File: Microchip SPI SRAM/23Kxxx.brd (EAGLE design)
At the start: 100 x 80 mm, 12 parts, among them IC2 23K**P, Q1 2SK1772

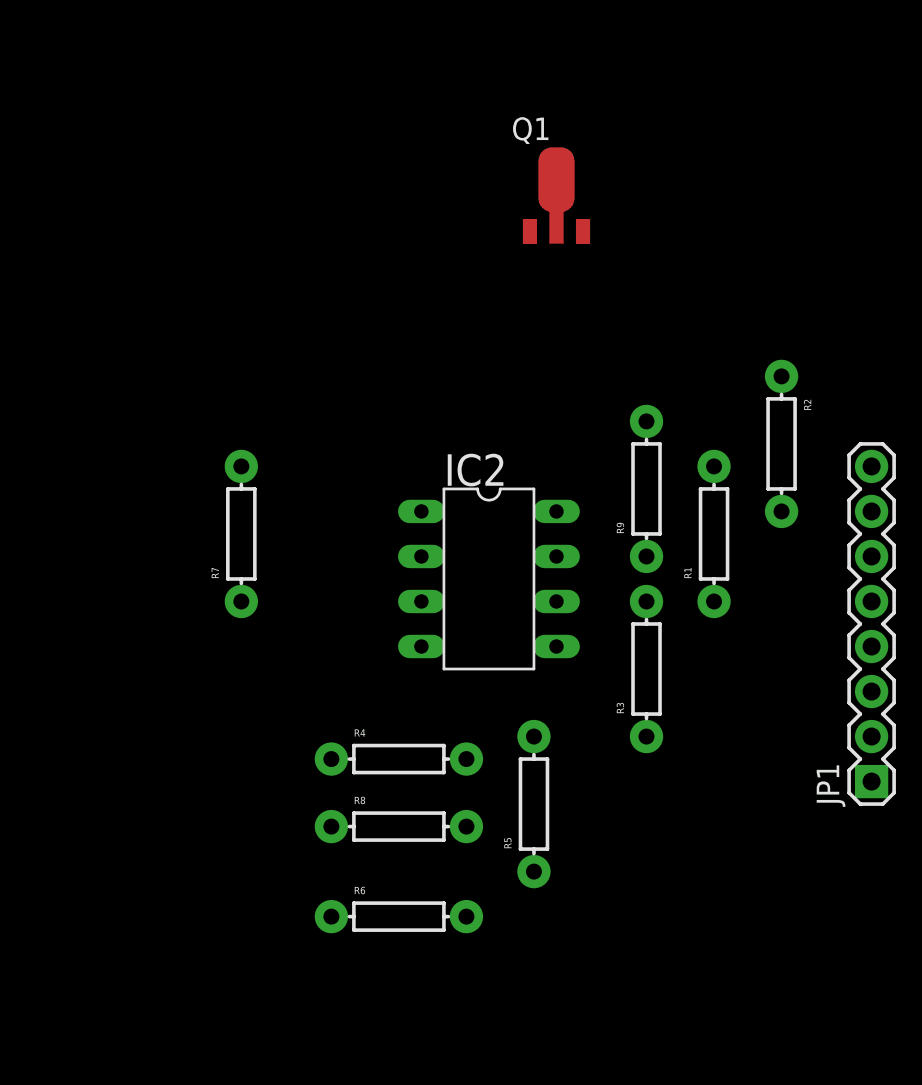
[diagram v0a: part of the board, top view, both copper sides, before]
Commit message: SPI SRAM pcb layout
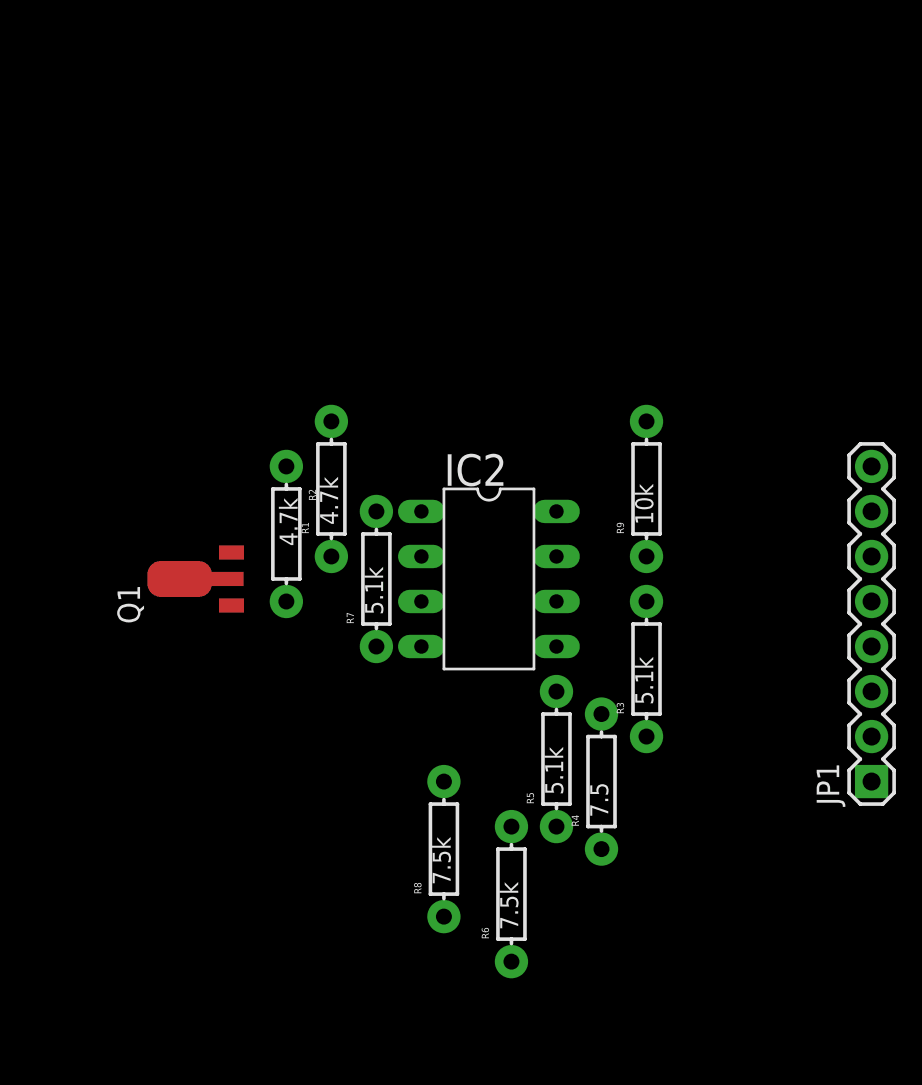
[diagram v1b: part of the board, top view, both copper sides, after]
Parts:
- R1, R2: value (none) -> 4.7k
- R3, R5, R7: value (none) -> 5.1k
- R4: value (none) -> 7.5
- R6, R8: value (none) -> 7.5k
- R9: value (none) -> 10k
- moved Q1 29.6 mm to (30.5, 30.5), turned to 90 degrees
- moved R2 28.4 mm to (35.6, 33.0)
- moved R1 21.7 mm to (38.1, 35.6)
- moved R4 11.5 mm to (53.3, 19.1), turned to 90 degrees
- moved R7 8.03 mm to (40.6, 30.5)
- moved R6 6.48 mm to (48.3, 12.7), turned to 90 degrees
- moved R8 2.84 mm to (44.5, 15.2), turned to 90 degrees
- moved R5 2.84 mm to (50.8, 20.3)
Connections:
- removed net N$2: JP1.3, Q1.3, R1.P$1
- new net N$1: JP1.3, Q1.2, Q1.2@1, R1.P$1
- net N$3: now also Q1.3; no longer Q1.2, Q1.2@1
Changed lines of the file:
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@@
 <elements>
 <element name="IC2" library="My Library" package="DIL8" value="23K**P" x="46.99" y="30.48" rot="R270"/>
-<element name="Q1" library="My Library" package="SOT89" value="2SK1772" x="50.8" y="52.07"/>
-<element name="R2" library="My Library" package="AXIAL-0.3" value="" x="63.5" y="38.1" rot="R270"/>
-<element name="R1" library="My Library" package="AXIAL-0.3" value="" x="59.69" y="33.02" rot="R90"/>
-<element name="R3" library="My Library" package="AXIAL-0.3" value="" x="55.88" y="25.4" rot="R90"/>
-<element name="R4" library="My Library" package="AXIAL-0.3" value="" x="41.91" y="20.32"/>
-<element name="R5" library="My Library" package="AXIAL-0.3" value="" x="49.53" y="17.78" rot="R90"/>
-<element name="R6" library="My Library" package="AXIAL-0.3" value="" x="41.91" y="11.43"/>
-<element name="R7" library="My Library" package="AXIAL-0.3" value="" x="33.02" y="33.02" rot="R90"/>
-<element name="R8" library="My Library" package="AXIAL-0.3" value="" x="41.91" y="16.51"/>
-<element name="R9" library="My Library" package="AXIAL-0.3" value="" x="55.88" y="35.56" rot="R90"/>
+<element name="Q1" library="My Library" package="SOT89" value="2SK1772" x="30.48" y="30.48" rot="R90"/>
+<element name="R2" library="My Library" package="AXIAL-0.3" value="4.7k" x="35.56" y="33.02" rot="R270"/>
+<element name="R1" library="My Library" package="AXIAL-0.3" value="4.7k" x="38.1" y="35.56" rot="R90"/>
+<element name="R3" library="My Library" package="AXIAL-0.3" value="5.1k" x="55.88" y="25.4" rot="R90"/>
+<element name="R4" library="My Library" package="AXIAL-0.3" value="7.5" x="53.34" y="19.05" rot="R90"/>
+<element name="R5" library="My Library" package="AXIAL-0.3" value="5.1k" x="50.8" y="20.32" rot="R90"/>
+<element name="R6" library="My Library" package="AXIAL-0.3" value="7.5k" x="48.26" y="12.7" rot="R90"/>
+<element name="R7" library="My Library" package="AXIAL-0.3" value="5.1k" x="40.64" y="30.48" rot="R90"/>
+<element name="R8" library="My Library" package="AXIAL-0.3" value="7.5k" x="44.45" y="15.24" rot="R90"/>
+<element name="R9" library="My Library" package="AXIAL-0.3" value="10k" x="55.88" y="35.56" rot="R90"/>
 <element name="JP1" library="SparkFun" package="1X08" value="" x="68.58" y="19.05" rot="R90"/>
 </elements>
@@
 <signal name="N$3">
 <contactref element="IC2" pad="2"/>
-<contactref element="Q1" pad="2"/>
-<contactref element="Q1" pad="2@1"/>
 <contactref element="R2" pad="P$1"/>
-<wire x1="50.8" y1="53.01" x2="50.8" y2="50.343" width="0" layer="19" extent="1-1"/>
-<wire x1="43.18" y1="31.75" x2="50.8" y2="50.343" width="0" layer="19" extent="1-1"/>
-<wire x1="63.5" y1="41.91" x2="50.8" y2="53.01" width="0" layer="19" extent="1-1"/>
+<contactref element="Q1" pad="3"/>
+<wire x1="35.56" y1="36.83" x2="43.18" y2="31.75" width="0" layer="19" extent="1-1"/>
+<wire x1="32.461" y1="31.979" x2="35.56" y2="36.83" width="0" layer="19" extent="1-1"/>
 </signal>
 <signal name="N$4">
 <contactref element="IC2" pad="1"/>
 <contactref element="R7" pad="P$2"/>
-<wire x1="33.02" y1="36.83" x2="43.18" y2="34.29" width="0" layer="19" extent="1-1"/>
+<wire x1="40.64" y1="34.29" x2="43.18" y2="34.29" width="0" layer="19" extent="1-1"/>
 </signal>
 <signal name="N$5">
@@
 <contactref element="JP1" pad="4"/>
 <wire x1="55.88" y1="21.59" x2="68.58" y2="26.67" width="0" layer="19" extent="1-1"/>
-<wire x1="45.72" y1="20.32" x2="55.88" y2="21.59" width="0" layer="19" extent="1-1"/>
+<wire x1="53.34" y1="22.86" x2="55.88" y2="21.59" width="0" layer="19" extent="1-1"/>
 </signal>
 <signal name="3.3V">
 <contactref element="Q1" pad="1"/>
-<contactref element="R2" pad="P$2"/>
 <contactref element="IC2" pad="8"/>
 <contactref element="R9" pad="P$2"/>
 <contactref element="JP1" pad="7"/>
-<wire x1="68.58" y1="34.29" x2="49.301" y2="50.089" width="0" layer="19" extent="1-1"/>
-<wire x1="63.5" y1="34.29" x2="68.58" y2="34.29" width="0" layer="19" extent="1-1"/>
-<wire x1="55.88" y1="39.37" x2="63.5" y2="34.29" width="0" layer="19" extent="1-1"/>
+<contactref element="R2" pad="P$2"/>
+<wire x1="55.88" y1="39.37" x2="68.58" y2="34.29" width="0" layer="19" extent="1-1"/>
 <wire x1="50.8" y1="34.29" x2="55.88" y2="39.37" width="0" layer="19" extent="1-1"/>
-</signal>
-<signal name="N$2">
-<contactref element="Q1" pad="3"/>
-<contactref element="R1" pad="P$1"/>
-<contactref element="JP1" pad="3"/>
-<wire x1="68.58" y1="24.13" x2="52.299" y2="50.089" width="0" layer="19" extent="1-1"/>
-<wire x1="59.69" y1="29.21" x2="68.58" y2="24.13" width="0" layer="19" extent="1-1"/>
+<wire x1="35.56" y1="29.21" x2="50.8" y2="34.29" width="0" layer="19" extent="1-1"/>
+<wire x1="32.461" y1="28.981" x2="35.56" y2="29.21" width="0" layer="19" extent="1-1"/>
 </signal>
 <signal name="5V">
 <contactref element="R1" pad="P$2"/>
 <contactref element="JP1" pad="8"/>
-<wire x1="68.58" y1="36.83" x2="59.69" y2="36.83" width="0" layer="19" extent="1-1"/>
+<wire x1="38.1" y1="39.37" x2="68.58" y2="36.83" width="0" layer="19" extent="1-1"/>
 </signal>
 <signal name="N$9">
 <contactref element="IC2" pad="5"/>
 <contactref element="R5" pad="P$2"/>
-<wire x1="49.53" y1="21.59" x2="50.8" y2="26.67" width="0" layer="19" extent="1-1"/>
+<wire x1="50.8" y1="24.13" x2="50.8" y2="26.67" width="0" layer="19" extent="1-1"/>
 </signal>
 <signal name="N$8">
@@
 <contactref element="R6" pad="P$2"/>
 <contactref element="JP1" pad="2"/>
-<wire x1="49.53" y1="13.97" x2="68.58" y2="21.59" width="0" layer="19" extent="1-1"/>
-<wire x1="45.72" y1="11.43" x2="49.53" y2="13.97" width="0" layer="19" extent="1-1"/>
+<wire x1="50.8" y1="16.51" x2="68.58" y2="21.59" width="0" layer="19" extent="1-1"/>
+<wire x1="48.26" y1="16.51" x2="50.8" y2="16.51" width="0" layer="19" extent="1-1"/>
 </signal>
 <signal name="N$11">
@@
 <contactref element="R8" pad="P$2"/>
 <contactref element="JP1" pad="1"/>
-<wire x1="45.72" y1="16.51" x2="68.58" y2="19.05" width="0" layer="19" extent="1-1"/>
-<wire x1="33.02" y1="29.21" x2="45.72" y2="16.51" width="0" layer="19" extent="1-1"/>
+<wire x1="44.45" y1="19.05" x2="68.58" y2="19.05" width="0" layer="19" extent="1-1"/>
+<wire x1="40.64" y1="26.67" x2="44.45" y2="19.05" width="0" layer="19" extent="1-1"/>
 </signal>
 <signal name="GND">
@@
 <contactref element="IC2" pad="4"/>
 <contactref element="JP1" pad="5"/>
-<wire x1="43.18" y1="26.67" x2="68.58" y2="29.21" width="0" layer="19" extent="1-1"/>
-<wire x1="38.1" y1="20.32" x2="43.18" y2="26.67" width="0" layer="19" extent="1-1"/>
-<wire x1="38.1" y1="16.51" x2="38.1" y2="20.32" width="0" layer="19" extent="1-1"/>
-<wire x1="38.1" y1="11.43" x2="38.1" y2="16.51" width="0" layer="19" extent="1-1"/>
+<wire x1="53.34" y1="15.24" x2="68.58" y2="29.21" width="0" layer="19" extent="1-1"/>
+<wire x1="48.26" y1="8.89" x2="53.34" y2="15.24" width="0" layer="19" extent="1-1"/>
+<wire x1="44.45" y1="11.43" x2="48.26" y2="8.89" width="0" layer="19" extent="1-1"/>
+<wire x1="43.18" y1="26.67" x2="53.34" y2="15.24" width="0" layer="19" extent="1-1"/>
+</signal>
+<signal name="N$1">
+<contactref element="JP1" pad="3"/>
+<contactref element="Q1" pad="2"/>
+<contactref element="Q1" pad="2@1"/>
+<contactref element="R1" pad="P$1"/>
+<wire x1="38.1" y1="31.75" x2="68.58" y2="24.13" width="0" layer="19" extent="1-1"/>
+<wire x1="32.207" y1="30.48" x2="38.1" y2="31.75" width="0" layer="19" extent="1-1"/>
+<wire x1="29.54" y1="30.48" x2="32.207" y2="30.48" width="0" layer="19" extent="1-1"/>
 </signal>
 </signals>
